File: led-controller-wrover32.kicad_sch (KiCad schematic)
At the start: 54 parts, among them J101 Molex PicoBlade 6-pin, J102 Molex PicoBlade 4-pin, J103 STATUS OUT, J104 USB_B_Micro, J105 POWER IN, J106 Molex PicoBlade 6-pin, J107 5V_LOGIC, Q101 UMH3N, Q102 BSS138, U101 USBUF02W6, U102 ESP32-S3-WROOM-2-N32R8V, U103 NTS0104BQ,115, U104 TCA9406ZYPR

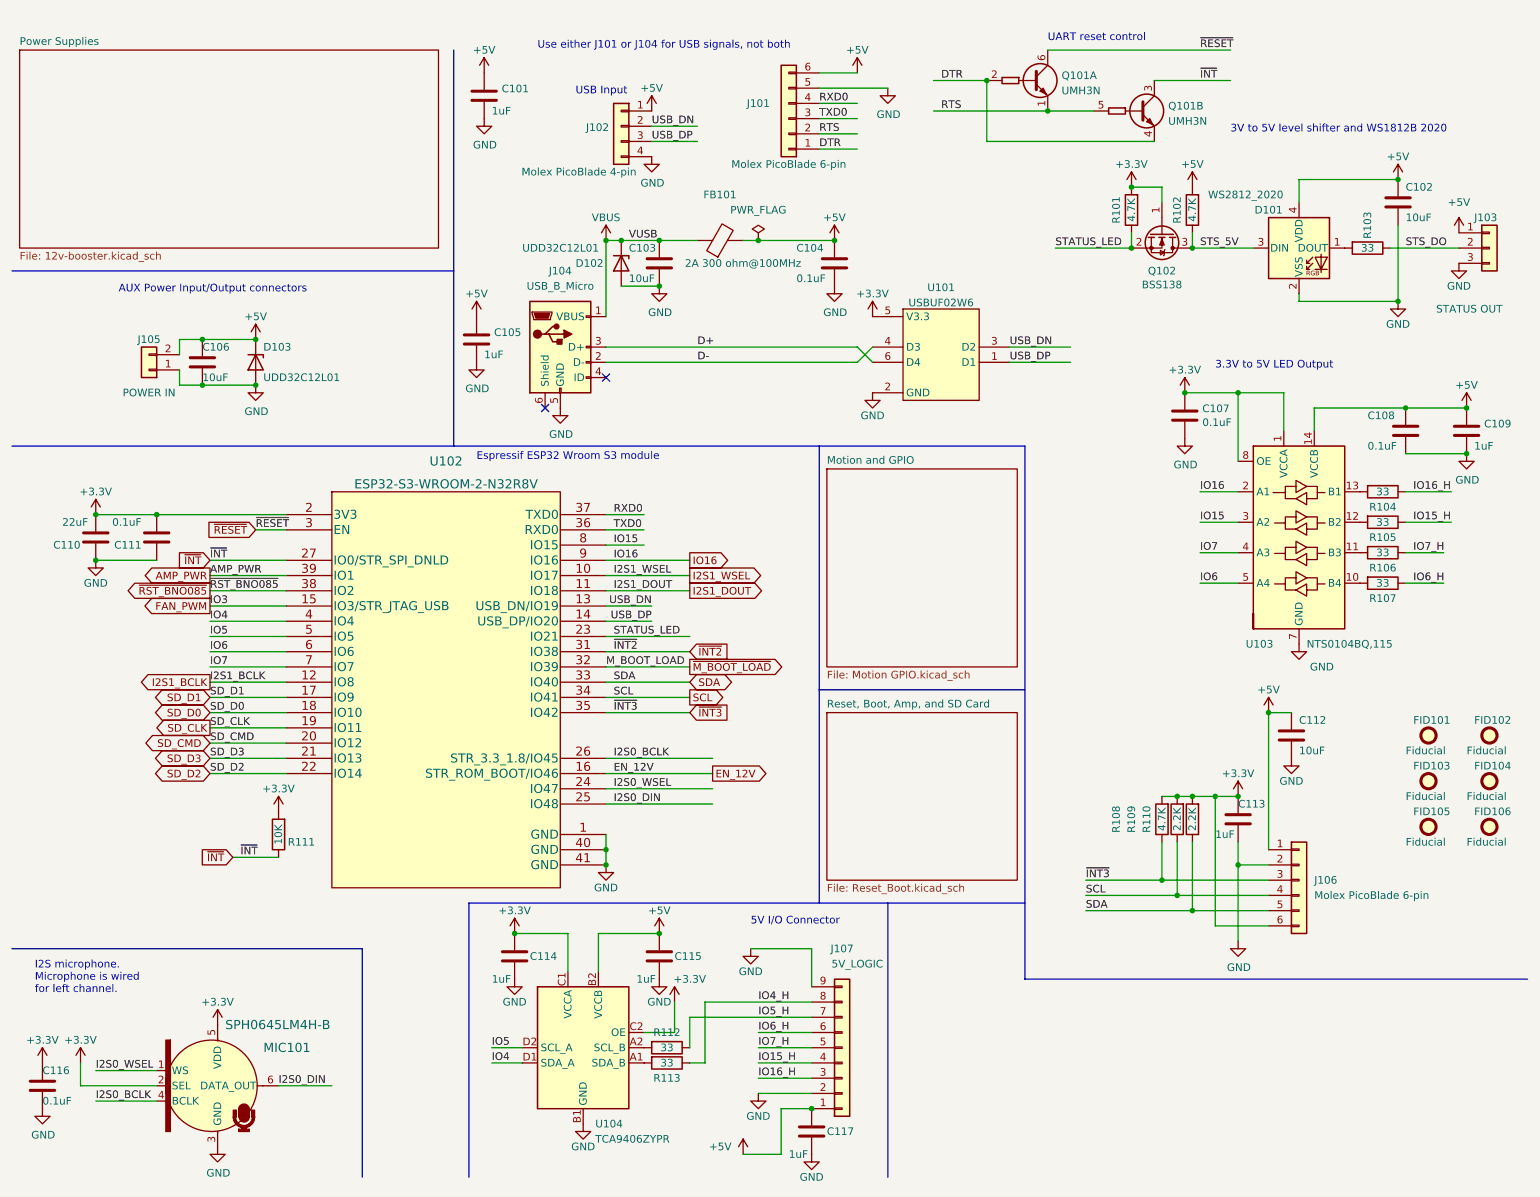
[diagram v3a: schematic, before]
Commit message: Switched to a different 12V booster chip and increased 12V from 500ma to 1A.
Also:
- Switched most 10uF capacitors to 0402 footprints.
- Other cleanup

Signed-off-by: Aaron Williams <aaron.w2@gmail.com>
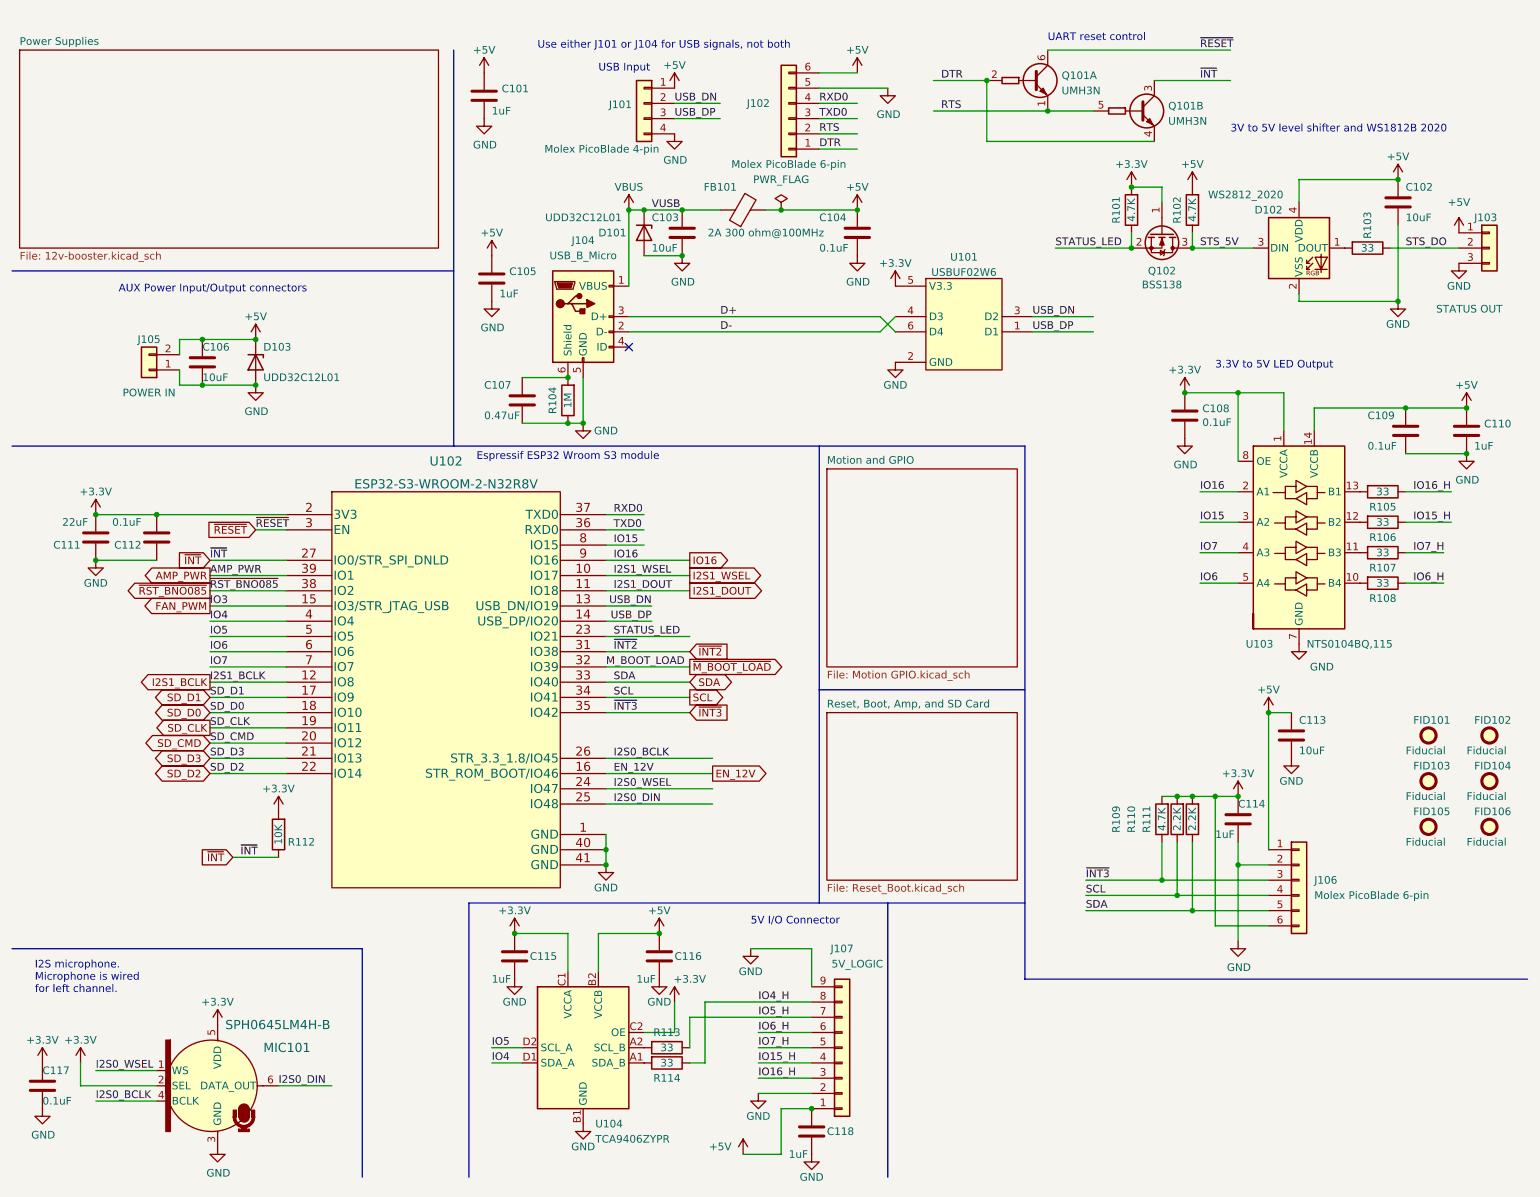
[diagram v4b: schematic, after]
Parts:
- added C107: 0.47uF, Capacitor_SMD:C_0402_1005Metric, symbol Device:C
- added R104: 1M, Resistor_SMD:R_0402_1005Metric, symbol Device:R
- C102, C103, C106: footprint Capacitor_SMD:C_0603_1608Metric -> Capacitor_SMD:C_0402_1005Metric; DESC (none) -> 10 µF ±20% 10V Ceramic Capacitor X5R 0402 (1005 Metric); DK_Datasheet_Link (none) -> https://media.digikey.com/pdf/Data%20Sheets/Samsung%20PDFs/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; DK_Detail_Page (none) -> https://www.digikey.com/en/products/detail/samsung-electro-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; Digi-Key_PN (none) -> 1276-1450-1-ND; MANUFACTURER (none) -> Samsung Electro-Mechanics; MFR (none) -> Samsung Electro-Mechanics; Manufacturer (none) -> Samsung Electro-Mechanics
- C113: renamed from C112; footprint Capacitor_SMD:C_0603_1608Metric -> Capacitor_SMD:C_0402_1005Metric; DESC (none) -> 10 µF ±20% 10V Ceramic Capacitor X5R 0402 (1005 Metric); DK_Datasheet_Link (none) -> https://media.digikey.com/pdf/Data%20Sheets/Samsung%20PDFs/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; DK_Detail_Page (none) -> https://www.digikey.com/en/products/detail/samsung-electro-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; Digi-Key_PN (none) -> 1276-1450-1-ND; MANUFACTURER (none) -> Samsung Electro-Mechanics; MFR (none) -> Samsung Electro-Mechanics; Manufacturer (none) -> Samsung Electro-Mechanics
- renumbered C107 to C108, C108 to C109, C109 to C110, C110 to C111, C111 to C112, C113 to C114, C114 to C115, C115 to C116, C116 to C117, C117 to C118, D102 to D101, D101 to D102, J102 to J101, J101 to J102, R104 to R105, R105 to R106, R106 to R107, R107 to R108, R108 to R109, R109 to R110, R110 to R111, R111 to R112, R112 to R113, R113 to R114
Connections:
- net GND: now also C107.2, R104.1
- net at J104.6 (Shield): now also C107.1, R104.2
- no-connect marks 2 -> 1
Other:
- moved on the sheet: C103, C104, C105, D101, FB101, J101, J104, U101

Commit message: Latest 4.0 settings for pcbway
Signed-off-by: Aaron Williams <aaron.w2@gmail.com>
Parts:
- removed C102, C103: 10uF, Capacitor_SMD:C_0402_1005Metric, symbol Device:C
- removed C116: 1uF, Capacitor_SMD:C_0402_1005Metric, symbol Device:C
- removed D101: UDD32C12L01, Diode_SMD:D_SOD-323, symbol Device:D_Zener
- removed Q102: BSS138, Package_TO_SOT_SMD:SOT-323_SC-70, symbol Transistor_FET:BSS138
- removed R101, R102: 4.7K, Resistor_SMD:R_0402_1005Metric, symbol Device:R
- removed R113, R114: 33, Resistor_SMD:R_0402_1005Metric, symbol Device:R
- removed U104: TCA9406ZYPR, Package_BGA:Texas_DSBGA-8_0.9x1.9mm_Layout2x4_P0.5mm, symbol Interface:TCA9406ZYPR
- added C101, C115: 1uF, Capacitor_SMD:C_0402_1005Metric, symbol Device:C
- added D101: TPD1E10B06DPYR, Diode_SMD:D_0402_1005Metric, symbol Device:D_TVS
- added JP101: IO4_IN_FILT, Jumper:SolderJumper-2_P1.3mm_Open_RoundedPad1.0x1.5mm, symbol Jumper:Jumper_2_Open
- added R107: 10K, Resistor_SMD:R_0402_1005Metric, symbol Device:R
- added TP101: TP +5_filtered, TestPoint:TestPoint_Pad_1.0x1.0mm, symbol Connector:TestPoint
- added TP102: TP +5_USB, TestPoint:TestPoint_Pad_1.0x1.0mm, symbol Connector:TestPoint
- added U101: TPS2001DDBVX, Package_TO_SOT_SMD:SOT-23-5, symbol Aaron:TPS2001DDBVX
- C102: renamed from C104; value 0.1uF -> 1uF; DESC (none) -> CAP CER 1UF 25V X5R 0402; Digi-Key_PN (none) -> 490-GRM155R61E105MA12JCT-ND; MANUFACTURER (none) -> Murata Electronics; MFR (none) -> Murata Electronics; MPN (none) -> GRM155R61E105MA12J; Manufacturer (none) -> Murata Electronics; Manufacturer Part Number (none) -> GRM155R61E105MA12J; SPN (none) -> 490-GRM155R61E105MA12JCT-ND; SPURL (none) -> https://www.digikey.com/en/products/detail/murata-electroni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
- C103: renamed from C101; DESC (none) -> CAP CER 1UF 25V X5R 0402; Digi-Key_PN (none) -> 490-GRM155R61E105MA12JCT-ND; MANUFACTURER (none) -> Murata Electronics; MFR (none) -> Murata Electronics; MPN (none) -> GRM155R61E105MA12J; Manufacturer (none) -> Murata Electronics; Manufacturer Part Number (none) -> GRM155R61E105MA12J; SPN (none) -> 490-GRM155R61E105MA12JCT-ND; SPURL (none) -> https://www.digikey.com/en/products/detail/murata-electroni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
- C104: renamed from C105; DESC (none) -> CAP CER 1UF 25V X5R 0402; Digi-Key_PN (none) -> 490-GRM155R61E105MA12JCT-ND; MANUFACTURER (none) -> Murata Electronics; MFR (none) -> Murata Electronics; MPN (none) -> GRM155R61E105MA12J; Manufacturer (none) -> Murata Electronics; Manufacturer Part Number (none) -> GRM155R61E105MA12J; SPN (none) -> 490-GRM155R61E105MA12JCT-ND; SPURL (none) -> https://www.digikey.com/en/products/detail/murata-electroni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
- C109: renamed from C110; DESC (none) -> CAP CER 1UF 25V X5R 0402; Digi-Key_PN (none) -> 490-GRM155R61E105MA12JCT-ND; MANUFACTURER (none) -> Murata Electronics; MFR (none) -> Murata Electronics; MPN (none) -> GRM155R61E105MA12J; Manufacturer (none) -> Murata Electronics; Manufacturer Part Number (none) -> GRM155R61E105MA12J; SPN (none) -> 490-GRM155R61E105MA12JCT-ND; SPURL (none) -> https://www.digikey.com/en/products/detail/murata-electroni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
- C110: renamed from C111; DESC (none) -> 22 µF ±20% 16V Ceramic Capacitor X5R 0603 (1608 Metric); DK_Datasheet_Link (none) -> https://media.digikey.com/pdf/Data%20Sheets/Samsung%20PDFs/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; DK_Detail_Page (none) -> https://www.digikey.com/en/products/detail/samsung-electro-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; Digi-Key_PN (none) -> 1276-7076-1-ND; MANUFACTURER (none) -> Samsung Electro-Mechanics; MFR (none) -> Samsung Electro-Mechanics; MPN (none) -> CL10A226MO7JZNC; Manufacturer (none) -> Samsung Electro-Mechanics; SPN (none) -> 1276-7076-1-ND; SPURL (none) -> https://www.digikey.com/en/products/detail/samsung-electro-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
- C113: renamed from C114; DESC CAP CER 1UF 10V X7R 0603 -> CAP CER 1UF 25V X5R 0402; Digi-Key_PN (none) -> 490-GRM155R61E105MA12JCT-ND; MANUFACTURER (none) -> Murata Electronics; MFR (none) -> Murata Electronics; MPN (none) -> GRM155R61E105MA12J; Manufacturer (none) -> Murata Electronics; Manufacturer Part Number (none) -> GRM155R61E105MA12J; SPN (none) -> 490-GRM155R61E105MA12JCT-ND; SPURL https://www.digikey.com/products/en?keywords=1276-1946-1-ND -> https://www.digikey.com/en/products/detail/murata-electroni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
- C114: renamed from C115; DESC (none) -> CAP CER 1UF 25V X5R 0402; Digi-Key_PN (none) -> 490-GRM155R61E105MA12JCT-ND; MANUFACTURER (none) -> Murata Electronics; MFR (none) -> Murata Electronics; MPN (none) -> GRM155R61E105MA12J; Manufacturer (none) -> Murata Electronics; Manufacturer Part Number (none) -> GRM155R61E105MA12J; SPN (none) -> 490-GRM155R61E105MA12JCT-ND; SPURL (none) -> https://www.digikey.com/en/products/detail/murata-electroni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
- C117: renamed from C118; DESC (none) -> CAP CER 1UF 25V X5R 0402; Digi-Key_PN (none) -> 490-GRM155R61E105MA12JCT-ND; MANUFACTURER (none) -> Murata Electronics; MFR (none) -> Murata Electronics; MPN (none) -> GRM155R61E105MA12J; Manufacturer (none) -> Murata Electronics; Manufacturer Part Number (none) -> GRM155R61E105MA12J; SPN (none) -> 490-GRM155R61E105MA12JCT-ND; SPURL (none) -> https://www.digikey.com/en/products/detail/murata-electroni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
- D102: footprint marbastlib-various:LED_WS2812_2020 -> Aaron:LED_WS2812_2020; MFR (none) -> World Semi
- FB101: MFR (none) -> Laird-Signal Integrity Products; SPN (none) -> 240-2374-1-ND; SPR (none) -> Digikey; SPURL (none) -> https://www.digikey.com/en/products/detail/laird-signal-int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
- J101: MANUFACTURER (none) -> Molex; MPN 0530470410 -> 0530470460; Manufacturer (none) -> Molex; Manufacturer Part Number (none) -> 0530470460; SPN WM1733-ND -> 900-0530470460-ND; SPURL https://www.digikey.com/en/products/detail/molex/0530470410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 -> https://www.digikey.com/en/products/detail/molex/0530470460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
- J102: DESC (none) -> Connector Header Through Hole 6 position 0.049" (1.25mm); Digi-Key_PN (none) -> 900-0530470660-ND; MPN (none) -> 0530470660; Manufacturer (none) -> Molex; Manufacturer Part Number (none) -> 0530470660; SPN (none) -> 900-0530470660-ND; SPR (none) -> Digikey; SPURL (none) -> https://www.digikey.com/en/products/detail/molex/0530470660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
- J103: MFR (none) -> JST Sales America Inc.; MPN (none) -> BM03B-SRSS-TBT(LF)(SN); SPN (none) -> 455-2957-1-ND; SPR (none) -> Digikey; SPURL (none) -> https://www.digikey.com/en/products/detail/jst-sales-americ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
- J104: MFR (none) -> Molex; MPN (none) -> 1050170001; SPN (none) -> WM1399CT-ND; SPR (none) -> Digikey; SPURL (none) -> https://www.digikey.com/en/products/detail/molex/1050170001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
- J105: MANUFACTURER (none) -> Molex
- J106: DESC (none) -> Connector Header Through Hole 6 position 0.049" (1.25mm); Digi-Key_PN (none) -> 900-0530470660-ND; MANUFACTURER (none) -> Molex; MFR (none) -> Molex; MPN (none) -> 0530470660; Manufacturer (none) -> Molex; Manufacturer Part Number (none) -> 0530470660; SPN (none) -> 900-0530470660-ND; SPR (none) -> Digikey; SPURL (none) -> https://www.digikey.com/en/products/detail/molex/0530470660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
- J107: DESC (none) -> Connector Header Surface Mount 9 position 0.039" (1.00mm); Digi-Key_PN (none) -> 455-1795-1-ND; MANUFACTURER (none) -> JST Sales America Inc.; MFR (none) -> JST Sales America Inc.; MPN (none) -> BM09B-SRSS-TB(LF)(SN); Manufacturer (none) -> JST Sales America Inc.; Manufacturer Part Number (none) -> BM09B-SRSS-TB(LF)(SN); SPN (none) -> 455-1795-1-ND; SPR (none) -> Digikey; SPURL (none) -> https://www.digikey.com/en/products/detail/jst-sales-americ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
- Q101: MFR (none) -> Rohm Semiconductor; MPN (none) -> UMH3NFHATN; SPN (none) -> UMH3NFHATNCT-ND; SPR (none) -> Digikey; SPURL (none) -> https://www.digikey.com/en/products/detail/rohm-semiconduct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
- R108: renamed from R109; value 4.7K -> 10K; DESC (none) -> 10 kOhms ±1% 0.063W, 1/16W Chip Resistor 0402 (1005 Metric)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; Digi-Key_PN (none) -> 311-10.0KLRCT-ND; MANUFACTURER (none) -> YAGEO; MFR (none) -> YAGEO; MPN (none) -> RC0402FR-0710KL; Manufacturer (none) -> YAGEO; Manufacturer Part Number (none) -> RC0402FR-0710KL; SPN CR0603-FX-4701ELFCT-ND -> 311-10.0KLRCT-ND; SPURL https://www.digikey.com/product-detail/en/bourns-inc/CR0603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 -> https://www.digikey.com/en/products/detail/yageo/RC0402FR-0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
- R111: renamed from R112; DESC (none) -> 10 kOhms ±1% 0.063W, 1/16W Chip Resistor 0402 (1005 Metric)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; Digi-Key_PN (none) -> 311-10.0KLRCT-ND; MANUFACTURER (none) -> YAGEO; MFR (none) -> YAGEO; MPN (none) -> RC0402FR-0710KL; Manufacturer (none) -> YAGEO; Manufacturer Part Number (none) -> RC0402FR-0710KL; SPN 541-2979-1-ND -> 311-10.0KLRCT-ND; SPURL https://www.digikey.com/products/en?keywords=541-2979-1-ND -> https://www.digikey.com/en/products/detail/yageo/RC0402FR-0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; Tolerance 5% -> (none)
- U102: renamed from U101; MFR (none) -> STMicroelectronics; MPN (none) -> USBUF02W6; SPN (none) -> 497-3743-1-ND; SPR (none) -> Digikey; SPURL (none) -> https://www.digikey.com/en/products/detail/stmicroelectroni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
- U103: renamed from U102; value ESP32-S3-WROOM-2-N32R8V -> ESP32-S3-WROOM-2-N32R8; footprint Aaron:ESP32-S3-WROOM-2-N32R8V -> Espressif:ESP32-S3-WROOM-2; MPN (none) -> ESP32-S3-WROOM-2-N32R8; SPN (none) -> 1965-ESP32-S3-WROOM-1-N16R8CT-ND; SPR (none) -> Digikey; SPURL (none) -> https://www.digikey.com/en/products/detail/espressif-system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
- U104: renamed from U103; SPN (none) -> 568-8407-1-ND; SPR (none) -> Digikey; SPURL (none) -> https://www.digikey.com/en/products/detail/nxp-usa-inc/NTS0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
- renumbered C106 to C105, C107 to C106, C108 to C107, C109 to C108, C112 to C111, C113 to C112, C117 to C116, R103 to R101, R104 to R102, R105 to R103, R106 to R104, R107 to R105, R108 to R106, R110 to R109, R111 to R110
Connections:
- net IO4_H is gone; now on net IO4: J107.8 (Pin_8)
- net IO5_H is gone; now on net IO5: J107.7 (Pin_7)
- net STS_5V is gone; now on net STATUS_LED: D102.3 (DIN)
- net +3V3: now also J107.9 (Pin_9)
- net +5V: now also C101.1, TP101.1, U101.1 (OUT); no longer C102.1, FB101.2
- net EN_12V: now also R107.2
- net GND: now also C101.2, C115.2, D101.2 (A2), R107.1, U101.2 (GND); no longer J107.9 (Pin_9)
- net IO4: now also JP101.2 (B)
- net VBUS: now also D101.1 (A1), TP102.1
- new net: C115.1, JP101.1 (A)
- new net FVUSB: C102.1, FB101.2, U101.4 (EN), U101.5 (IN)
- no-connect marks 1 -> 2
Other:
- note added: "Current Limiter"
- note added: "Note GPIO46 requires a pull-down to allow for download booting."
- note added: "Strapping: GPIO45: 0 (not used) GPIO0: 1 SPI boot (prog button) GPIO46: 0 Print during boot/enable download GPIO3: 1 JTAG USB"
- moved on the sheet: C102, C103, C108, C109, C112, C113, C114, FB101, J101, J102, J106, U102

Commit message: Minor fixes.
Signed-off-by: Aaron Williams <aaron.w2@gmail.com>
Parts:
- FID101, FID102, FID103, FID104, FID105, FID106, TP101, TP102: now left out of the parts list
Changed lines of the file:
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@@
   )
   (symbol (lib_id "Mechanical:Fiducial") (at 248.92 137.16 0) (unit 1)
-    (in_bom yes) (on_board yes)
+    (in_bom no) (on_board yes)
     (property "Reference" "FID103" (id 0) (at 246.38 134.62 0)
       (effects (font (size 1.27 1.27)) (justify left))
@@
   )
   (symbol (lib_id "Mechanical:Fiducial") (at 259.08 129.54 0) (unit 1)
-    (in_bom yes) (on_board yes)
+    (in_bom no) (on_board yes)
     (property "Reference" "FID102" (id 0) (at 256.54 127 0)
       (effects (font (size 1.27 1.27)) (justify left))
@@
   )
   (symbol (lib_id "Mechanical:Fiducial") (at 259.08 137.16 0) (unit 1)
-    (in_bom yes) (on_board yes)
+    (in_bom no) (on_board yes)
     (property "Reference" "FID104" (id 0) (at 256.54 134.62 0)
       (effects (font (size 1.27 1.27)) (justify left))
@@
   )
   (symbol (lib_id "Mechanical:Fiducial") (at 248.92 129.54 0) (unit 1)
-    (in_bom yes) (on_board yes)
+    (in_bom no) (on_board yes)
     (property "Reference" "FID101" (id 0) (at 246.38 127 0)
       (effects (font (size 1.27 1.27)) (justify left))
@@
   )
   (symbol (lib_id "Connector:TestPoint") (at 120.65 71.12 180) (unit 1)
-    (in_bom yes) (on_board yes) (fields_autoplaced)
+    (in_bom no) (on_board yes) (fields_autoplaced)
     (property "Reference" "TP101" (id 0) (at 123.19 73.1519 0)
       (effects (font (size 1.27 1.27)) (justify right))
@@
   )
   (symbol (lib_id "Connector:TestPoint") (at 138.43 71.12 180) (unit 1)
-    (in_bom yes) (on_board yes) (fields_autoplaced)
+    (in_bom no) (on_board yes) (fields_autoplaced)
     (property "Reference" "TP102" (id 0) (at 140.97 73.1519 0)
       (effects (font (size 1.27 1.27)) (justify right))
@@
   )
   (symbol (lib_id "Mechanical:Fiducial") (at 259.08 144.78 0) (unit 1)
-    (in_bom yes) (on_board yes)
+    (in_bom no) (on_board yes)
     (property "Reference" "FID106" (id 0) (at 256.54 142.24 0)
       (effects (font (size 1.27 1.27)) (justify left))
@@
   )
   (symbol (lib_id "Mechanical:Fiducial") (at 248.92 144.78 0) (unit 1)
-    (in_bom yes) (on_board yes)
+    (in_bom no) (on_board yes)
     (property "Reference" "FID105" (id 0) (at 246.38 142.24 0)
       (effects (font (size 1.27 1.27)) (justify left))
@@
     )
     (path "/00000000-0000-0000-0000-00005dd65482/00000000-0000-0000-0000-00005ec189c0"
-      (reference "Q301") (unit 1) (value "BSS138") (footprint "Package_TO_SOT_SMD:SOT-323_SC-70")
+      (reference "Q301") (unit 1) (value "BSS138PW,115") (footprint "Package_TO_SOT_SMD:SOT-323_SC-70")
     )
     (path "/db7d5c34-b074-413f-ad06-63dd211660ee/dcc3da9a-89fa-4442-8dc5-a68551f42a6c"
@@
       (reference "TP301") (unit 1) (value "~{RESET}") (footprint "TestPoint:TestPoint_Pad_1.0x1.0mm")
     )
+    (path "/db7d5c34-b074-413f-ad06-63dd211660ee/0b0416c3-f67c-44fb-8023-2d057f4d2663"
+      (reference "TP401") (unit 1) (value "~{BNO_RST}") (footprint "TestPoint:TestPoint_Pad_1.0x1.0mm")
+    )
     (path "/5914596c-e34a-4f04-b746-45b6f8653853"
